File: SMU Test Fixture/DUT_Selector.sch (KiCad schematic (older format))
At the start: 17 parts, among them J3 Conn_02x16_Odd_Even, K11 EC2-12SNU, K12 EC2-12SNU, K13 EC2-12SNU, K14 EC2-12SNU, K15 EC2-12SNU, K16 EC2-12SNU, K17 EC2-12SNU, K18 EC2-12SNU, K19 EC2-12SNU, K20 EC2-12SNU, K21 EC2-12SNU, K22 EC2-12SNU, K23 EC2-12SNU, K24 EC2-12SNU, K25 EC2-12SNU, K26 EC2-12SNU

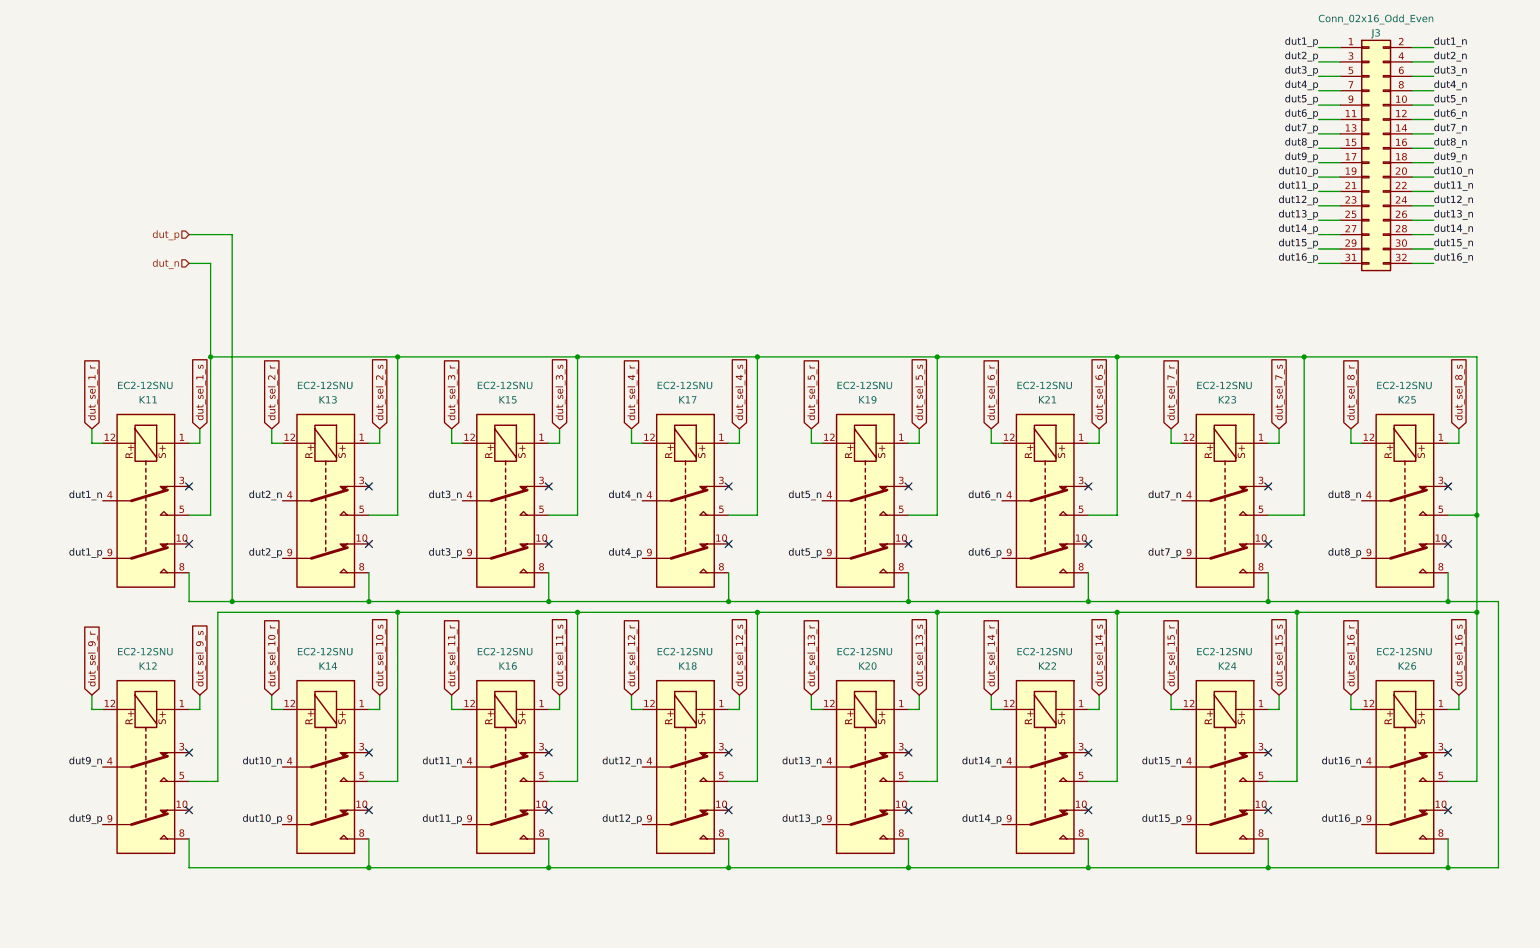
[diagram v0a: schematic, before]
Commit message: Elminate extra scope cal relay, re-organize relays, re-annotate, ERC
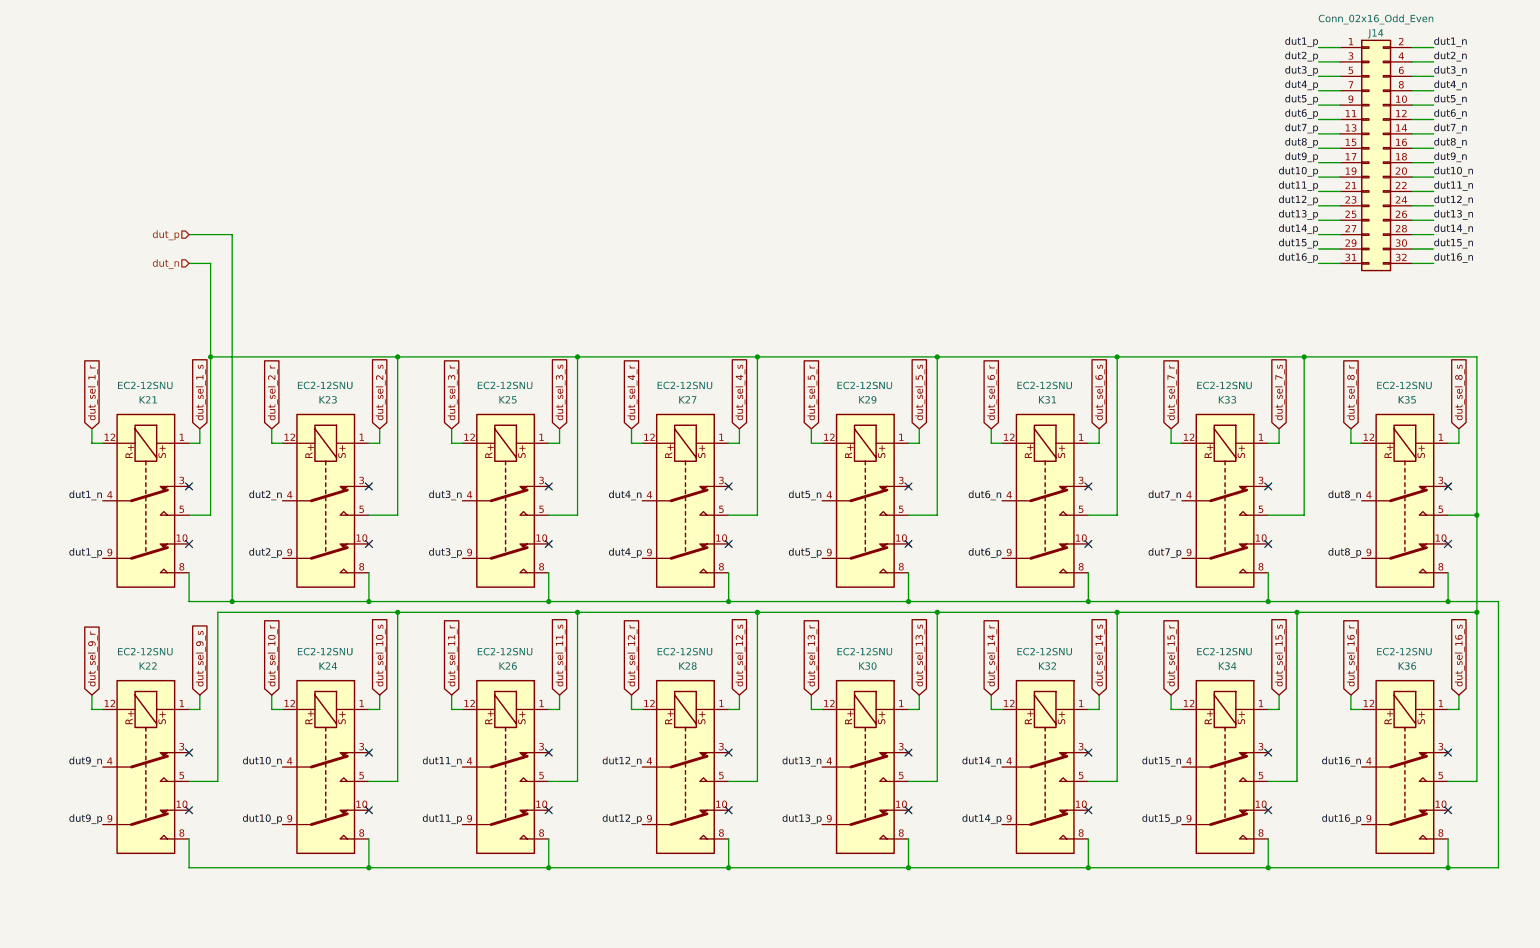
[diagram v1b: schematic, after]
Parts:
- renumbered J3 to J14, K11 to K21, K12 to K22, K13 to K23, K14 to K24, K15 to K25, K16 to K26, K17 to K27, K18 to K28, K19 to K29, K20 to K30, K21 to K31, K22 to K32, K23 to K33, K24 to K34, K25 to K35, K26 to K36
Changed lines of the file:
@@
 $Descr A4 11693 8268
 encoding utf-8
-Sheet 4 8
+Sheet 8 8
 Title ""
 Date ""
@@
 AR Path="/5FE064B5/6021E5C6" Ref="J?"  Part="1"
 AR Path="/6021E5C6" Ref="J?"  Part="1"
-AR Path="/600C9795/6021E5C6" Ref="J3"  Part="1"
-F 0 "J3" H 9950 2250 50  0000 C CNN
+AR Path="/600C9795/6021E5C6" Ref="J14"  Part="1"
+F 0 "J14" H 9950 2250 50  0000 C CNN
 F 1 "Conn_02x16_Odd_Even" H 9950 2350 50  0000 C CNN
 F 2 "" H 9900 1450 50  0001 C CNN
@@
 dut16_n
 $Comp
-L Relay:EE2-12SNUH K13
+L Relay:EE2-12SNUH K23
 U 1 1 5FC14030
 P 2650 3900
-F 0 "K13" V 1950 3850 50  0000 L CNN
+F 0 "K23" V 1950 3850 50  0000 L CNN
 F 1 "EC2-12SNU" V 1850 3700 50  0000 L CNN
 F 2 "Relay_SMD:Relay_DPDT_Kemet_EE2_NUH" H 2650 3900 50  0001 C CNN
@@
 $EndComp
 $Comp
-L Relay:EE2-12SNUH K15
+L Relay:EE2-12SNUH K25
 U 1 1 5FC1816C
 P 3900 3900
-F 0 "K15" V 3200 3850 50  0000 L CNN
+F 0 "K25" V 3200 3850 50  0000 L CNN
 F 1 "EC2-12SNU" V 3100 3700 50  0000 L CNN
 F 2 "Relay_SMD:Relay_DPDT_Kemet_EE2_NUH" H 3900 3900 50  0001 C CNN
@@
 $EndComp
 $Comp
-L Relay:EE2-12SNUH K19
+L Relay:EE2-12SNUH K29
 U 1 1 5FC25C02
 P 6400 3900
-F 0 "K19" V 5700 3850 50  0000 L CNN
+F 0 "K29" V 5700 3850 50  0000 L CNN
 F 1 "EC2-12SNU" V 5600 3700 50  0000 L CNN
 F 2 "Relay_SMD:Relay_DPDT_Kemet_EE2_NUH" H 6400 3900 50  0001 C CNN
@@
 $EndComp
 $Comp
-L Relay:EE2-12SNUH K21
+L Relay:EE2-12SNUH K31
 U 1 1 5FC25C08
 P 7650 3900
-F 0 "K21" V 6950 3850 50  0000 L CNN
+F 0 "K31" V 6950 3850 50  0000 L CNN
 F 1 "EC2-12SNU" V 6850 3700 50  0000 L CNN
 F 2 "Relay_SMD:Relay_DPDT_Kemet_EE2_NUH" H 7650 3900 50  0001 C CNN
@@
 $EndComp
 $Comp
-L Relay:EE2-12SNUH K23
+L Relay:EE2-12SNUH K33
 U 1 1 5FC25C0E
 P 8900 3900
-F 0 "K23" V 8200 3850 50  0000 L CNN
+F 0 "K33" V 8200 3850 50  0000 L CNN
 F 1 "EC2-12SNU" V 8100 3700 50  0000 L CNN
 F 2 "Relay_SMD:Relay_DPDT_Kemet_EE2_NUH" H 8900 3900 50  0001 C CNN
@@
 $EndComp
 $Comp
-L Relay:EE2-12SNUH K25
+L Relay:EE2-12SNUH K35
 U 1 1 5FC25C14
 P 10150 3900
-F 0 "K25" V 9450 3850 50  0000 L CNN
+F 0 "K35" V 9450 3850 50  0000 L CNN
 F 1 "EC2-12SNU" V 9350 3700 50  0000 L CNN
 F 2 "Relay_SMD:Relay_DPDT_Kemet_EE2_NUH" H 10150 3900 50  0001 C CNN
@@
 $EndComp
 $Comp
-L Relay:EE2-12SNUH K12
+L Relay:EE2-12SNUH K22
 U 1 1 5FC38B22
 P 1400 5750
-F 0 "K12" V 700 5700 50  0000 L CNN
+F 0 "K22" V 700 5700 50  0000 L CNN
 F 1 "EC2-12SNU" V 600 5550 50  0000 L CNN
 F 2 "Relay_SMD:Relay_DPDT_Kemet_EE2_NUH" H 1400 5750 50  0001 C CNN
@@
 $EndComp
 $Comp
-L Relay:EE2-12SNUH K14
+L Relay:EE2-12SNUH K24
 U 1 1 5FC38B28
 P 2650 5750
-F 0 "K14" V 1950 5700 50  0000 L CNN
+F 0 "K24" V 1950 5700 50  0000 L CNN
 F 1 "EC2-12SNU" V 1850 5550 50  0000 L CNN
 F 2 "Relay_SMD:Relay_DPDT_Kemet_EE2_NUH" H 2650 5750 50  0001 C CNN
@@
 $EndComp
 $Comp
-L Relay:EE2-12SNUH K20
+L Relay:EE2-12SNUH K30
 U 1 1 5FC38B3A
 P 6400 5750
-F 0 "K20" V 5700 5700 50  0000 L CNN
+F 0 "K30" V 5700 5700 50  0000 L CNN
 F 1 "EC2-12SNU" V 5600 5550 50  0000 L CNN
 F 2 "Relay_SMD:Relay_DPDT_Kemet_EE2_NUH" H 6400 5750 50  0001 C CNN
@@
 $EndComp
 $Comp
-L Relay:EE2-12SNUH K22
+L Relay:EE2-12SNUH K32
 U 1 1 5FC38B40
 P 7650 5750
-F 0 "K22" V 6950 5700 50  0000 L CNN
+F 0 "K32" V 6950 5700 50  0000 L CNN
 F 1 "EC2-12SNU" V 6850 5550 50  0000 L CNN
 F 2 "Relay_SMD:Relay_DPDT_Kemet_EE2_NUH" H 7650 5750 50  0001 C CNN
@@
 $EndComp
 $Comp
-L Relay:EE2-12SNUH K24
+L Relay:EE2-12SNUH K34
 U 1 1 5FC38B46
 P 8900 5750
-F 0 "K24" V 8200 5700 50  0000 L CNN
+F 0 "K34" V 8200 5700 50  0000 L CNN
 F 1 "EC2-12SNU" V 8100 5550 50  0000 L CNN
 F 2 "Relay_SMD:Relay_DPDT_Kemet_EE2_NUH" H 8900 5750 50  0001 C CNN
@@
 $EndComp
 $Comp
-L Relay:EE2-12SNUH K26
+L Relay:EE2-12SNUH K36
 U 1 1 5FC38B4C
 P 10150 5750
-F 0 "K26" V 9450 5700 50  0000 L CNN
+F 0 "K36" V 9450 5700 50  0000 L CNN
 F 1 "EC2-12SNU" V 9350 5550 50  0000 L CNN
 F 2 "Relay_SMD:Relay_DPDT_Kemet_EE2_NUH" H 10150 5750 50  0001 C CNN
@@
 dut14_p
 $Comp
-L Relay:EE2-12SNUH K11
+L Relay:EE2-12SNUH K21
 U 1 1 60CA6945
 P 1400 3900
-F 0 "K11" V 700 3850 50  0000 L CNN
+F 0 "K21" V 700 3850 50  0000 L CNN
 F 1 "EC2-12SNU" V 600 3700 50  0000 L CNN
 F 2 "Relay_SMD:Relay_DPDT_Kemet_EE2_NUH" H 1400 3900 50  0001 C CNN
@@
 $EndComp
 $Comp
-L Relay:EE2-12SNUH K17
+L Relay:EE2-12SNUH K27
 U 1 1 5FC18172
 P 5150 3900
-F 0 "K17" V 4450 3850 50  0000 L CNN
+F 0 "K27" V 4450 3850 50  0000 L CNN
 F 1 "EC2-12SNU" V 4350 3700 50  0000 L CNN
 F 2 "Relay_SMD:Relay_DPDT_Kemet_EE2_NUH" H 5150 3900 50  0001 C CNN
@@
 	10525 5350 10450 5350
 $Comp
-L Relay:EE2-12SNUH K16
+L Relay:EE2-12SNUH K26
 U 1 1 5FC38B2E
 P 3900 5750
-F 0 "K16" V 3200 5700 50  0000 L CNN
+F 0 "K26" V 3200 5700 50  0000 L CNN
 F 1 "EC2-12SNU" V 3100 5550 50  0000 L CNN
 F 2 "Relay_SMD:Relay_DPDT_Kemet_EE2_NUH" H 3900 5750 50  0001 C CNN
@@
 	1850 2250 1850 2900
 $Comp
-L Relay:EE2-12SNUH K18
+L Relay:EE2-12SNUH K28
 U 1 1 5FC38B34
 P 5150 5750
-F 0 "K18" V 4450 5700 50  0000 L CNN
+F 0 "K28" V 4450 5700 50  0000 L CNN
 F 1 "EC2-12SNU" V 4350 5550 50  0000 L CNN
 F 2 "Relay_SMD:Relay_DPDT_Kemet_EE2_NUH" H 5150 5750 50  0001 C CNN

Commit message: Switch to 28V txfrmr, nix preregs, nix 5V for AD2, switch to 12V relay power.
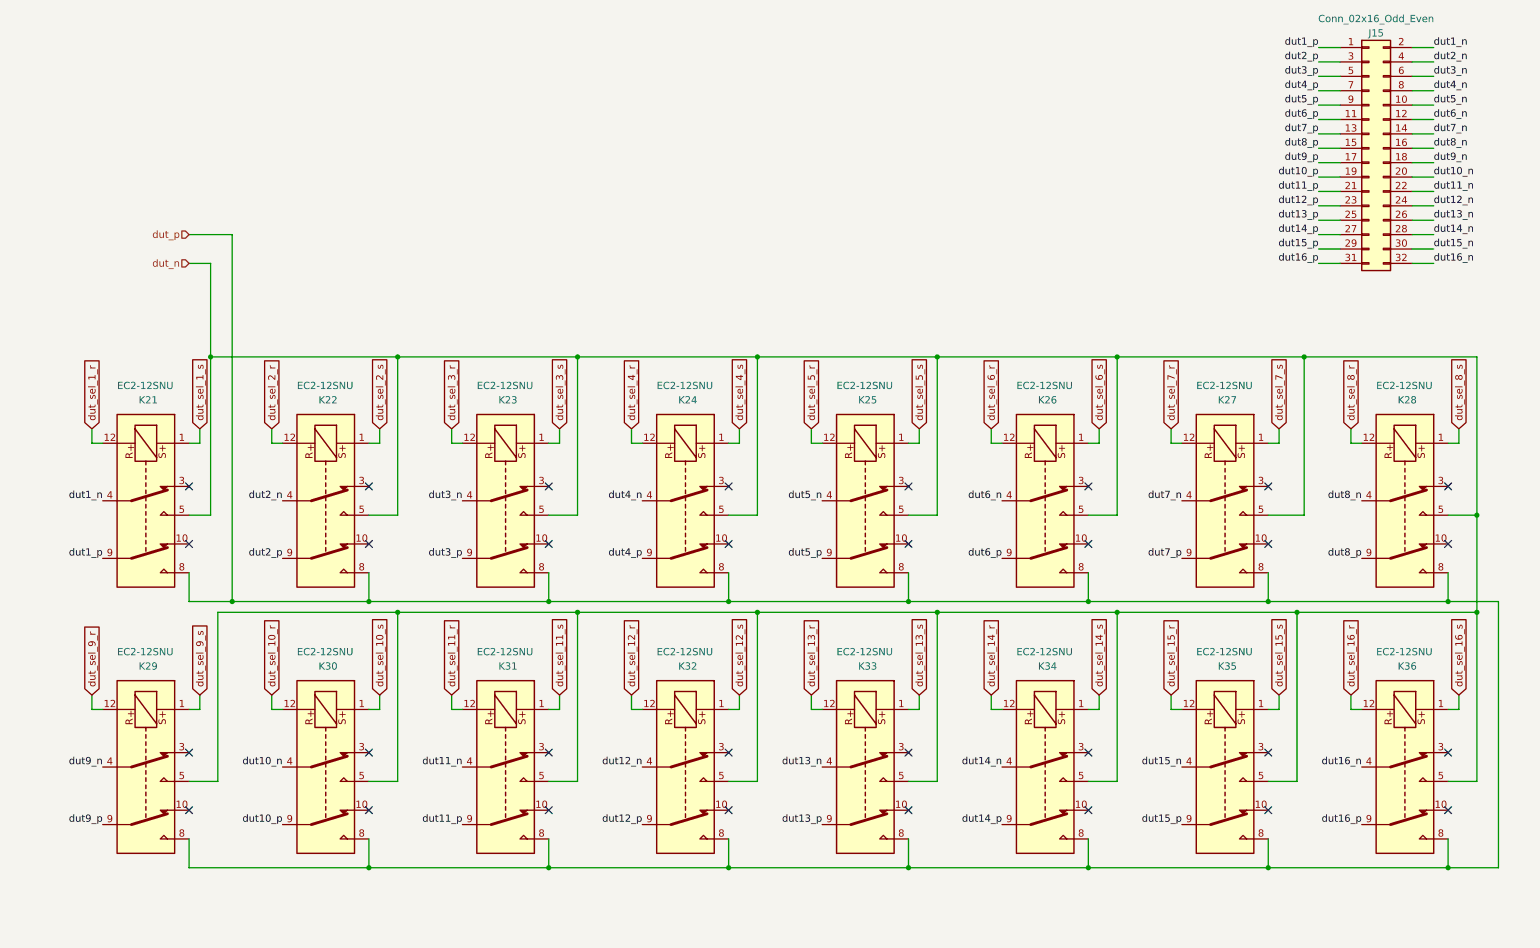
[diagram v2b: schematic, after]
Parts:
- renumbered J14 to J15, K23 to K22, K25 to K23, K27 to K24, K29 to K25, K31 to K26, K33 to K27, K35 to K28, K22 to K29, K24 to K30, K26 to K31, K28 to K32, K30 to K33, K32 to K34, K34 to K35
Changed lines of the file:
@@
 AR Path="/5FE064B5/6021E5C6" Ref="J?"  Part="1"
 AR Path="/6021E5C6" Ref="J?"  Part="1"
-AR Path="/600C9795/6021E5C6" Ref="J14"  Part="1"
-F 0 "J14" H 9950 2250 50  0000 C CNN
+AR Path="/600C9795/6021E5C6" Ref="J15"  Part="1"
+F 0 "J15" H 9950 2250 50  0000 C CNN
 F 1 "Conn_02x16_Odd_Even" H 9950 2350 50  0000 C CNN
 F 2 "" H 9900 1450 50  0001 C CNN
@@
 dut16_n
 $Comp
-L Relay:EE2-12SNUH K23
+L Relay:EE2-12SNUH K22
 U 1 1 5FC14030
 P 2650 3900
-F 0 "K23" V 1950 3850 50  0000 L CNN
+F 0 "K22" V 1950 3850 50  0000 L CNN
 F 1 "EC2-12SNU" V 1850 3700 50  0000 L CNN
 F 2 "Relay_SMD:Relay_DPDT_Kemet_EE2_NUH" H 2650 3900 50  0001 C CNN
@@
 $EndComp
 $Comp
-L Relay:EE2-12SNUH K25
+L Relay:EE2-12SNUH K23
 U 1 1 5FC1816C
 P 3900 3900
-F 0 "K25" V 3200 3850 50  0000 L CNN
+F 0 "K23" V 3200 3850 50  0000 L CNN
 F 1 "EC2-12SNU" V 3100 3700 50  0000 L CNN
 F 2 "Relay_SMD:Relay_DPDT_Kemet_EE2_NUH" H 3900 3900 50  0001 C CNN
@@
 $EndComp
 $Comp
-L Relay:EE2-12SNUH K29
+L Relay:EE2-12SNUH K25
 U 1 1 5FC25C02
 P 6400 3900
-F 0 "K29" V 5700 3850 50  0000 L CNN
+F 0 "K25" V 5700 3850 50  0000 L CNN
 F 1 "EC2-12SNU" V 5600 3700 50  0000 L CNN
 F 2 "Relay_SMD:Relay_DPDT_Kemet_EE2_NUH" H 6400 3900 50  0001 C CNN
@@
 $EndComp
 $Comp
-L Relay:EE2-12SNUH K31
+L Relay:EE2-12SNUH K26
 U 1 1 5FC25C08
 P 7650 3900
-F 0 "K31" V 6950 3850 50  0000 L CNN
+F 0 "K26" V 6950 3850 50  0000 L CNN
 F 1 "EC2-12SNU" V 6850 3700 50  0000 L CNN
 F 2 "Relay_SMD:Relay_DPDT_Kemet_EE2_NUH" H 7650 3900 50  0001 C CNN
@@
 $EndComp
 $Comp
-L Relay:EE2-12SNUH K33
+L Relay:EE2-12SNUH K27
 U 1 1 5FC25C0E
 P 8900 3900
-F 0 "K33" V 8200 3850 50  0000 L CNN
+F 0 "K27" V 8200 3850 50  0000 L CNN
 F 1 "EC2-12SNU" V 8100 3700 50  0000 L CNN
 F 2 "Relay_SMD:Relay_DPDT_Kemet_EE2_NUH" H 8900 3900 50  0001 C CNN
@@
 $EndComp
 $Comp
-L Relay:EE2-12SNUH K35
+L Relay:EE2-12SNUH K28
 U 1 1 5FC25C14
 P 10150 3900
-F 0 "K35" V 9450 3850 50  0000 L CNN
+F 0 "K28" V 9450 3850 50  0000 L CNN
 F 1 "EC2-12SNU" V 9350 3700 50  0000 L CNN
 F 2 "Relay_SMD:Relay_DPDT_Kemet_EE2_NUH" H 10150 3900 50  0001 C CNN
@@
 $EndComp
 $Comp
-L Relay:EE2-12SNUH K22
+L Relay:EE2-12SNUH K29
 U 1 1 5FC38B22
 P 1400 5750
-F 0 "K22" V 700 5700 50  0000 L CNN
+F 0 "K29" V 700 5700 50  0000 L CNN
 F 1 "EC2-12SNU" V 600 5550 50  0000 L CNN
 F 2 "Relay_SMD:Relay_DPDT_Kemet_EE2_NUH" H 1400 5750 50  0001 C CNN
@@
 $EndComp
 $Comp
-L Relay:EE2-12SNUH K24
+L Relay:EE2-12SNUH K30
 U 1 1 5FC38B28
 P 2650 5750
-F 0 "K24" V 1950 5700 50  0000 L CNN
+F 0 "K30" V 1950 5700 50  0000 L CNN
 F 1 "EC2-12SNU" V 1850 5550 50  0000 L CNN
 F 2 "Relay_SMD:Relay_DPDT_Kemet_EE2_NUH" H 2650 5750 50  0001 C CNN
@@
 $EndComp
 $Comp
-L Relay:EE2-12SNUH K30
+L Relay:EE2-12SNUH K33
 U 1 1 5FC38B3A
 P 6400 5750
-F 0 "K30" V 5700 5700 50  0000 L CNN
+F 0 "K33" V 5700 5700 50  0000 L CNN
 F 1 "EC2-12SNU" V 5600 5550 50  0000 L CNN
 F 2 "Relay_SMD:Relay_DPDT_Kemet_EE2_NUH" H 6400 5750 50  0001 C CNN
@@
 $EndComp
 $Comp
-L Relay:EE2-12SNUH K32
+L Relay:EE2-12SNUH K34
 U 1 1 5FC38B40
 P 7650 5750
-F 0 "K32" V 6950 5700 50  0000 L CNN
+F 0 "K34" V 6950 5700 50  0000 L CNN
 F 1 "EC2-12SNU" V 6850 5550 50  0000 L CNN
 F 2 "Relay_SMD:Relay_DPDT_Kemet_EE2_NUH" H 7650 5750 50  0001 C CNN
@@
 $EndComp
 $Comp
-L Relay:EE2-12SNUH K34
+L Relay:EE2-12SNUH K35
 U 1 1 5FC38B46
 P 8900 5750
-F 0 "K34" V 8200 5700 50  0000 L CNN
+F 0 "K35" V 8200 5700 50  0000 L CNN
 F 1 "EC2-12SNU" V 8100 5550 50  0000 L CNN
 F 2 "Relay_SMD:Relay_DPDT_Kemet_EE2_NUH" H 8900 5750 50  0001 C CNN
@@
 $EndComp
 $Comp
-L Relay:EE2-12SNUH K27
+L Relay:EE2-12SNUH K24
 U 1 1 5FC18172
 P 5150 3900
-F 0 "K27" V 4450 3850 50  0000 L CNN
+F 0 "K24" V 4450 3850 50  0000 L CNN
 F 1 "EC2-12SNU" V 4350 3700 50  0000 L CNN
 F 2 "Relay_SMD:Relay_DPDT_Kemet_EE2_NUH" H 5150 3900 50  0001 C CNN
@@
 	10525 5350 10450 5350
 $Comp
-L Relay:EE2-12SNUH K26
+L Relay:EE2-12SNUH K31
 U 1 1 5FC38B2E
 P 3900 5750
-F 0 "K26" V 3200 5700 50  0000 L CNN
+F 0 "K31" V 3200 5700 50  0000 L CNN
 F 1 "EC2-12SNU" V 3100 5550 50  0000 L CNN
 F 2 "Relay_SMD:Relay_DPDT_Kemet_EE2_NUH" H 3900 5750 50  0001 C CNN
@@
 	1850 2250 1850 2900
 $Comp
-L Relay:EE2-12SNUH K28
+L Relay:EE2-12SNUH K32
 U 1 1 5FC38B34
 P 5150 5750
-F 0 "K28" V 4450 5700 50  0000 L CNN
+F 0 "K32" V 4450 5700 50  0000 L CNN
 F 1 "EC2-12SNU" V 4350 5550 50  0000 L CNN
 F 2 "Relay_SMD:Relay_DPDT_Kemet_EE2_NUH" H 5150 5750 50  0001 C CNN

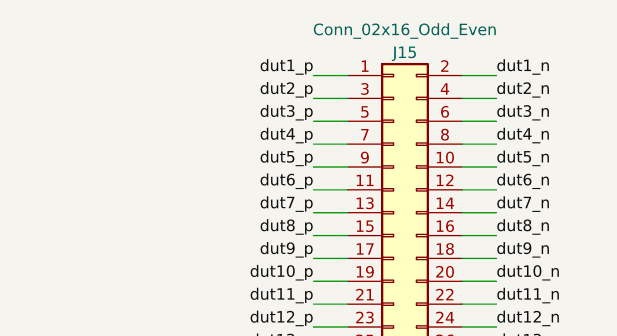
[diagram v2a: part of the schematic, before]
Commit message: Reannotate, power supply schematic improvements, begin power supply layout.
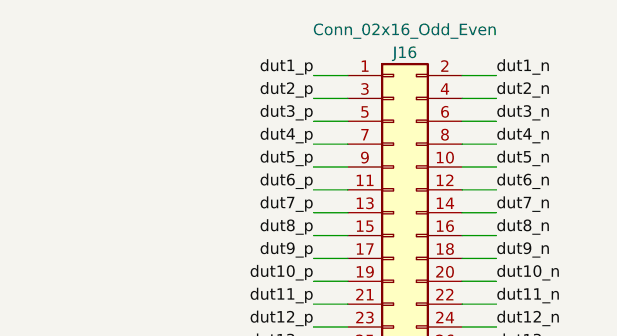
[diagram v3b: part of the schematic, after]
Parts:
- renumbered J15 to J16
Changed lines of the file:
@@
 AR Path="/5FE064B5/6021E5C6" Ref="J?"  Part="1"
 AR Path="/6021E5C6" Ref="J?"  Part="1"
-AR Path="/600C9795/6021E5C6" Ref="J15"  Part="1"
-F 0 "J15" H 9950 2250 50  0000 C CNN
+AR Path="/600C9795/6021E5C6" Ref="J16"  Part="1"
+F 0 "J16" H 9950 2250 50  0000 C CNN
 F 1 "Conn_02x16_Odd_Even" H 9950 2350 50  0000 C CNN
 F 2 "" H 9900 1450 50  0001 C CNN

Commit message: Redesign with analog switches.
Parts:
- removed K21, K22, K23, K24, K25, K26, K27, K28, K29, K30, K31, K32, K33, K34, K35, K36: EC2-12SNU, Relay_SMD:Relay_DPDT_Kemet_EE2_NUH, symbol Relay:EE2-12SNUH
- added U? (x6): ADGS1408, Package_CSP:LFCSP-24-1EP_4x4mm_P0.5mm_EP2.5x2.5mm, symbol MAGI_Symbols:ADGS1408
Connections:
- net labels added: vdut
- net labels removed: dut_sel_10_r, dut_sel_10_s, dut_sel_11_r, dut_sel_11_s, dut_sel_12_r, dut_sel_12_s, dut_sel_13_r, dut_sel_13_s, dut_sel_14_r, dut_sel_14_s, dut_sel_15_r, dut_sel_15_s, dut_sel_16_r, dut_sel_16_s, dut_sel_1_r, dut_sel_1_s, dut_sel_2_r, dut_sel_2_s, dut_sel_3_r, dut_sel_3_s, dut_sel_4_r, dut_sel_4_s, dut_sel_5_r, dut_sel_5_s, dut_sel_6_r, dut_sel_6_s, dut_sel_7_r, dut_sel_7_s, dut_sel_8_r, dut_sel_8_s, dut_sel_9_r, dut_sel_9_s
- wire segments 181 -> 72
- no-connect marks 32 -> 0
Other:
- moved on the sheet: J?

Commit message: Add analog switch power connections.
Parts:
- added C? (x6): 1u, symbol Device:C_Small
- added R? (x6): 100R, symbol Device:R_Small_US
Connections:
- net labels added: +15V, -15V, GND
- wire segments 72 -> 150
